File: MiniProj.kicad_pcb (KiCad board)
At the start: 2 copper layers, 22 parts, among them SW1_UP1 SW_Push_Dual, SW2_DOWN1 SW_Push_Dual, SW3_LEFT1 SW_Push_Dual, SW4_RIGHT1 SW_Push_Dual, SW5_RESET1 SW_Push_Dual, U1 STM32F051R8Tx

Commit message: PLPCB
Rev 1
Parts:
- added C8: 1uF, Capacitor_SMD:C_0402_1005Metric, F.Cu at (194.3, 47.0)
- added J1: 1935161, digikey-footprints:Terminal_Block_D1.3mm_P5mm, F.Cu at (254.0, 48.3)
- added J2: Conn_01x16_Male, Connector_PinHeader_2.54mm:PinHeader_1x16_P2.54mm_Vertical, F.Cu at (242.6, 64.8)
- added J3: Conn_01x16_Male, Connector_PinHeader_2.54mm:PinHeader_1x16_P2.54mm_Vertical, F.Cu at (184.2, 88.9)
- added J4: Conn_01x16_Male, Connector_PinHeader_2.54mm:PinHeader_1x16_P2.54mm_Vertical, F.Cu at (176.5, 35.6)
- added J5: Conn_01x16_Male, Connector_PinHeader_2.54mm:PinHeader_1x16_P2.54mm_Vertical, F.Cu at (191.8, 34.3)
- added PS1: IA0503S_copy, PDS1-S3-S3-M_1:CONV_PDS1-S3-S3-M, F.Cu at (240.0, 50.8)
- added R10: 10k, Resistor_SMD:R_0402_1005Metric, F.Cu at (195.6, 40.6)
- added R11: 510, Resistor_SMD:R_0402_1005Metric, F.Cu at (195.6, 43.2)
- C1, C2, C3, C4, C6, C7: footprint Capacitor_SMD:C_0201_0603Metric -> Capacitor_SMD:C_0402_1005Metric
- moved R1 62.8 mm to (135.9, 69.4)
- moved R5 58.7 mm to (99.1, 90.2)
- moved C1 57.9 mm to (141.0, 74.9)
- moved C3 57.9 mm to (101.6, 97.8)
- moved C4 57.9 mm to (163.8, 95.2)
- moved C7 57.9 mm to (154.9, 54.6)
- moved R2 57.9 mm to (141.0, 71.1)
- moved R7 57.9 mm to (161.3, 87.6)
- moved R8 57.9 mm to (163.3, 91.4)
- moved R9 57.9 mm to (154.9, 51.3), turned to 0 degrees
- moved SW1_UP1 57.9 mm to (128.3, 76.2)
- moved SW2_DOWN1 57.9 mm to (128.3, 92.7)
- moved SW3_LEFT1 57.9 mm to (109.2, 92.7)
- moved SW4_RIGHT1 57.9 mm to (147.3, 92.7)
- moved SW5_RESET1 57.9 mm to (143.5, 53.3)
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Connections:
- R1 pad 2: +3V0 -> VDD
- R4 pad 2: +3V0 -> VDD
- R5 pad 2: +3V0 -> VDD
- R7 pad 2: +3V0 -> VDD
- U1 pad 1: Net-(U1-Pad1) -> VDD
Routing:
- net VDD: track 0.00 -> 410.9 mm, vias 0 -> 10
- net GND: track 0.00 -> 403.0 mm, vias 0 -> 7
- net PC2: track 0.00 -> 123.6 mm, vias 0 -> 2
- net PC1: track 0.00 -> 101.8 mm, vias 0 -> 1
- net PC3: track 0.00 -> 69.1 mm
- net PC0: track 0.00 -> 69.0 mm
- net PB12: track 0.00 -> 60.8 mm
- net NRST: track 0.00 -> 60.0 mm, vias 0 -> 1
- net PB13: track 0.00 -> 59.3 mm
- net PB14: track 0.00 -> 57.7 mm
- net PB15: track 0.00 -> 56.1 mm
- net PC6: track 0.00 -> 54.5 mm
- net PC7: track 0.00 -> 52.9 mm
- net PC8: track 0.00 -> 51.3 mm
- net PC9: track 0.00 -> 49.7 mm
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- added copper zone on F.Cu, net GND
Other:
- board text added: "ECE 362 Group 1 - Rev 1 Josh Panos - Tommy Rhodes - Cooper Campbell - Joseph"

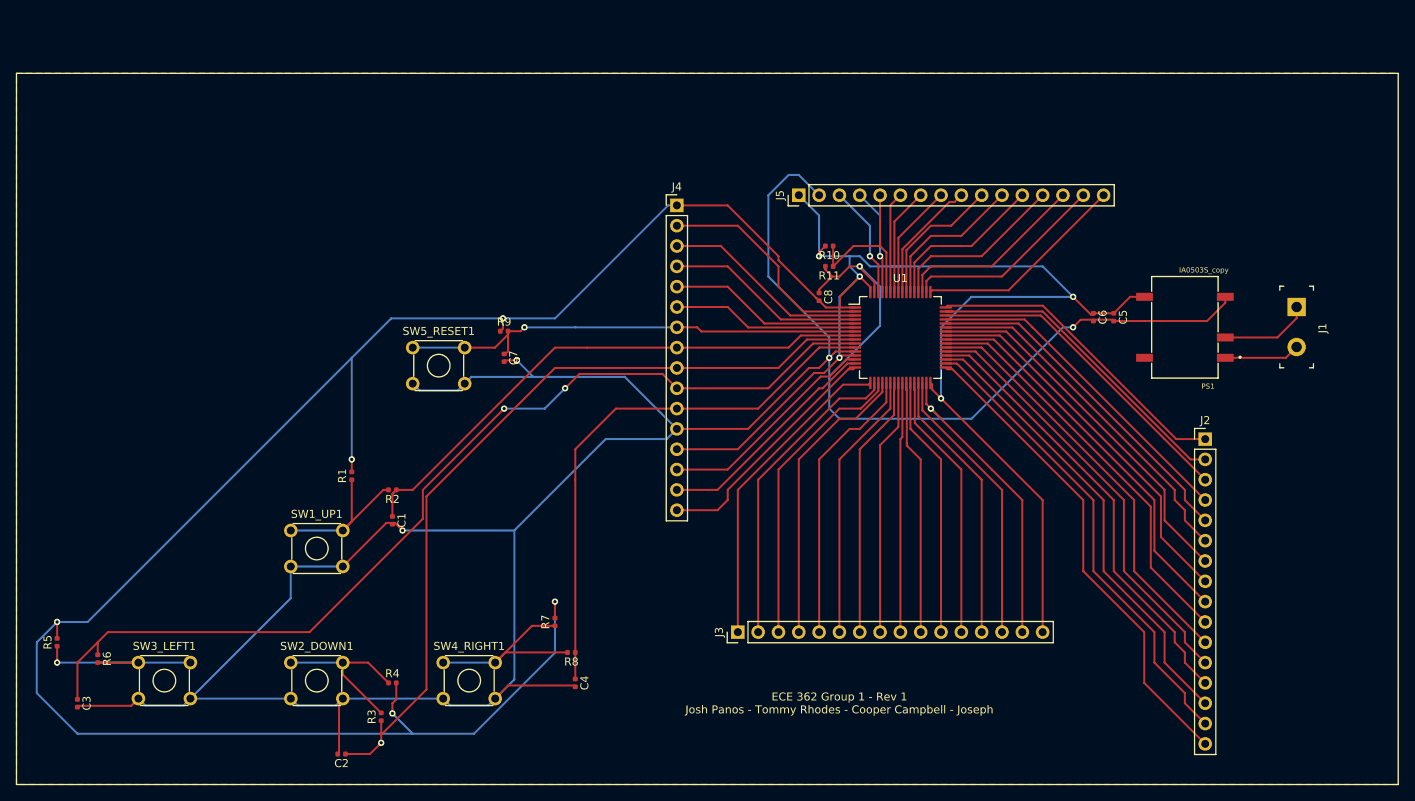
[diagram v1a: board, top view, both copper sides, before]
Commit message: BIgger pads
Change R and C
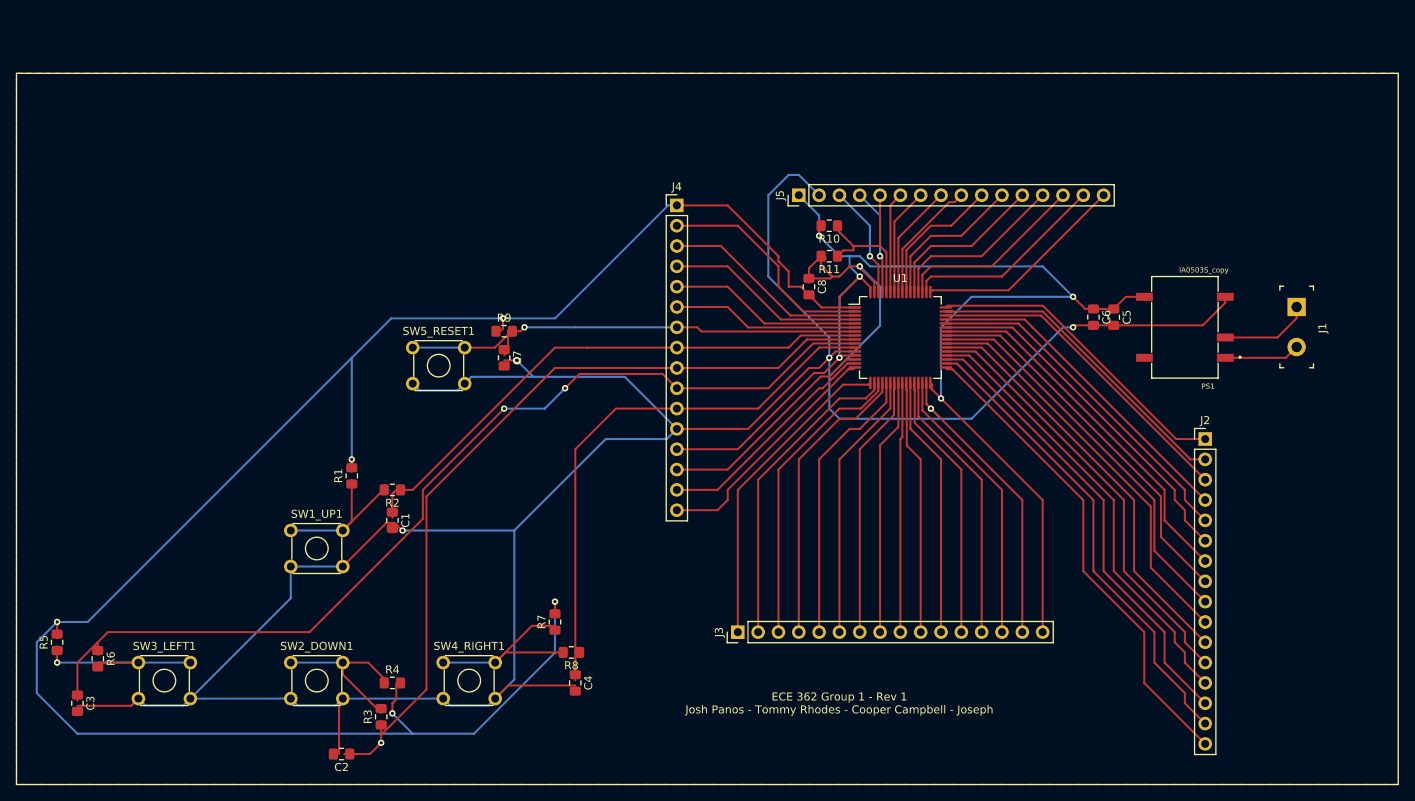
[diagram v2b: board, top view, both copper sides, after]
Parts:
- C1, C2, C3, C4, C5, C6, C7, C8: footprint Capacitor_SMD:C_0402_1005Metric -> Capacitor_SMD:C_0805_2012Metric_Pad1.15x1.40mm_HandSolder
- R1, R10, R11, R2, R3, R4, R5, R6, R7, R8, R9: footprint Resistor_SMD:R_0402_1005Metric -> Resistor_SMD:R_0805_2012Metric_Pad1.15x1.40mm_HandSolder
- moved R10 2.54 mm to (195.6, 38.1)
- moved C8 1.80 mm to (193.0, 45.7)
- moved R11 1.27 mm to (195.6, 41.9)
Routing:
- net GND: track 403.0 -> 408.9 mm
- net VDD: track 410.9 -> 409.8 mm
